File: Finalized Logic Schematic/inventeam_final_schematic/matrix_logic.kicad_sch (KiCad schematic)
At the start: 27 parts, among them J1 USB_C_Receptacle_PowerOnly_6P, J2 Conn_01x02, J3 Screw_Terminal_01x04, J4 JST Female, J5 JST Male, J6 JST Female, J7 JST Male, U1 LM66100DCK, U2 LM66100DCK

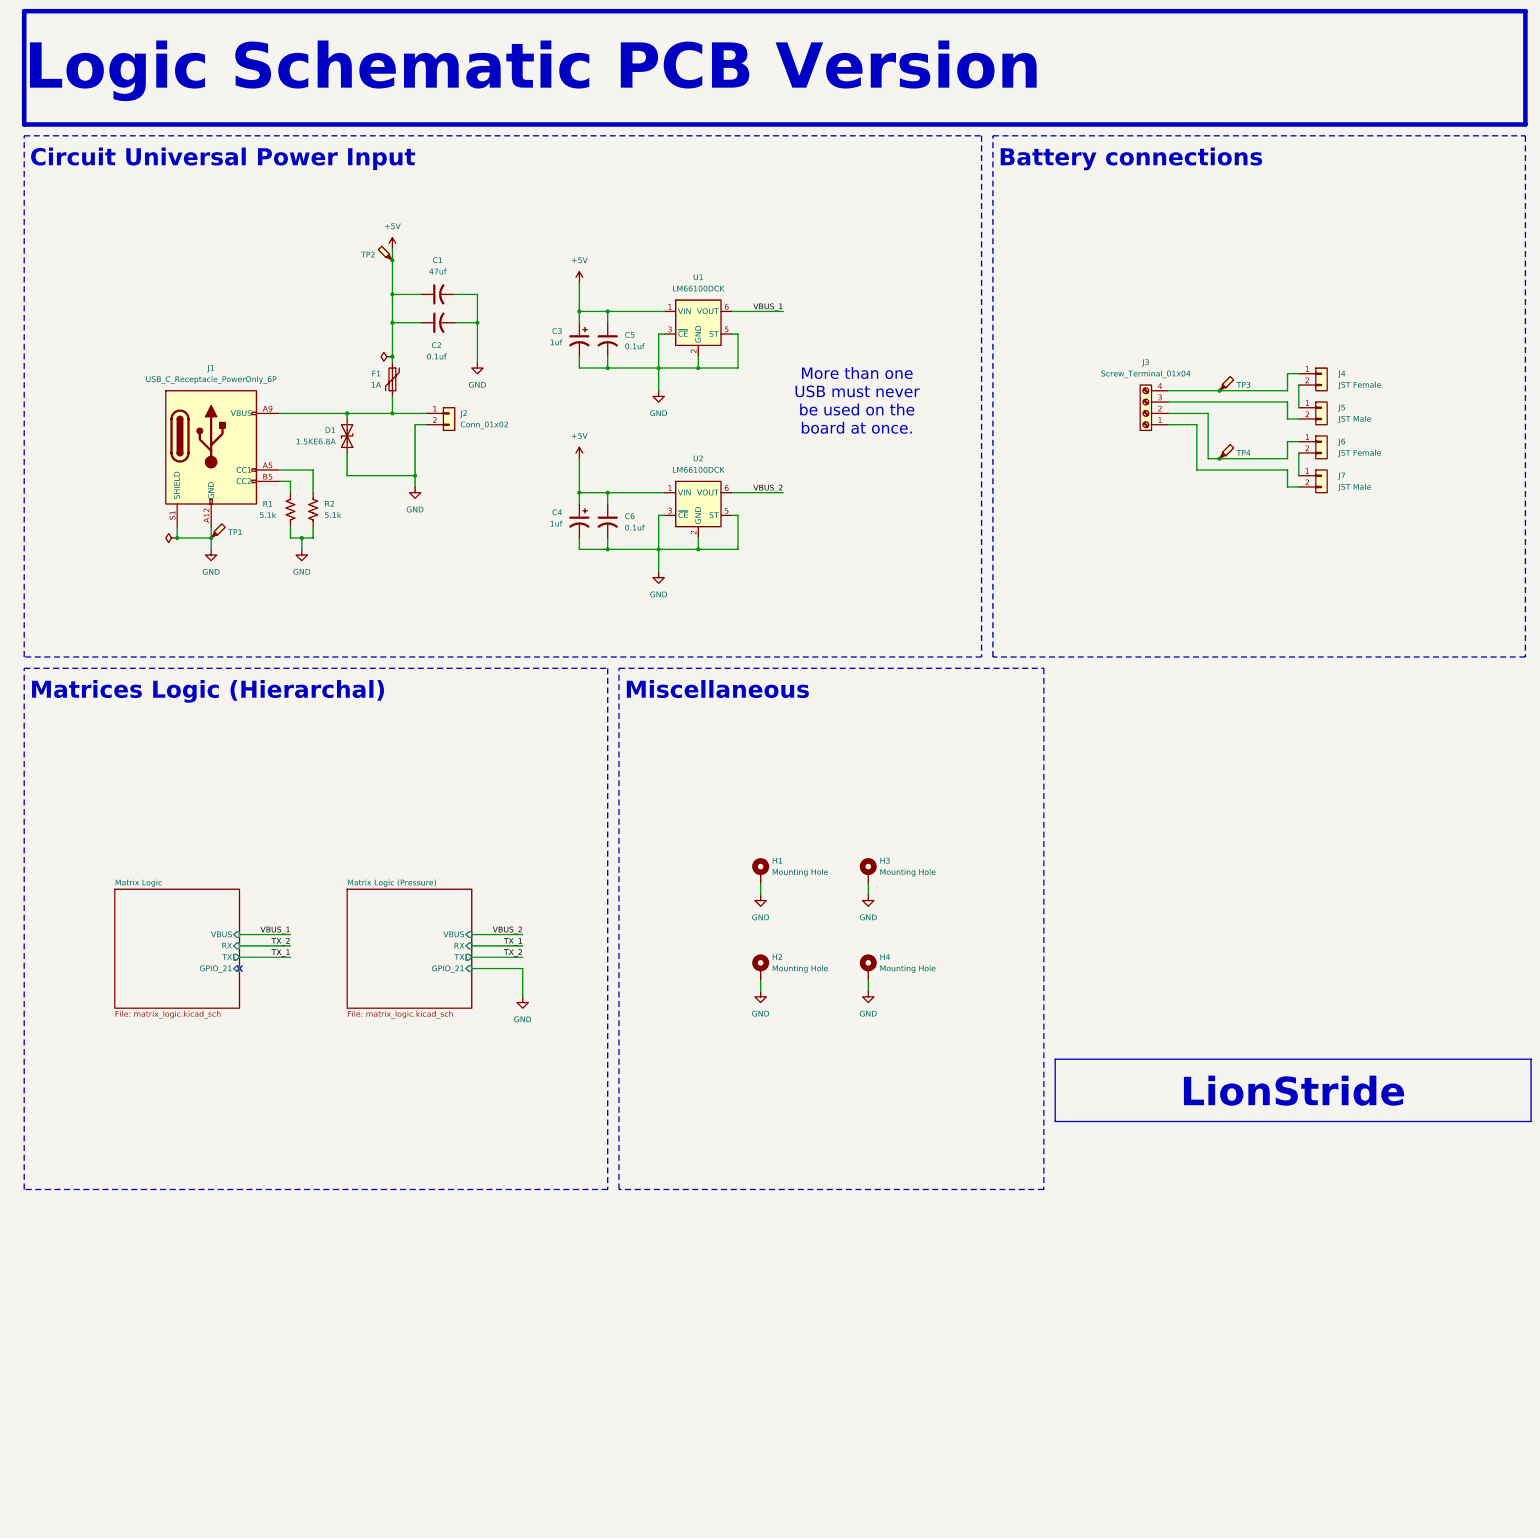
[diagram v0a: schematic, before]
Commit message: Logic schematic V2
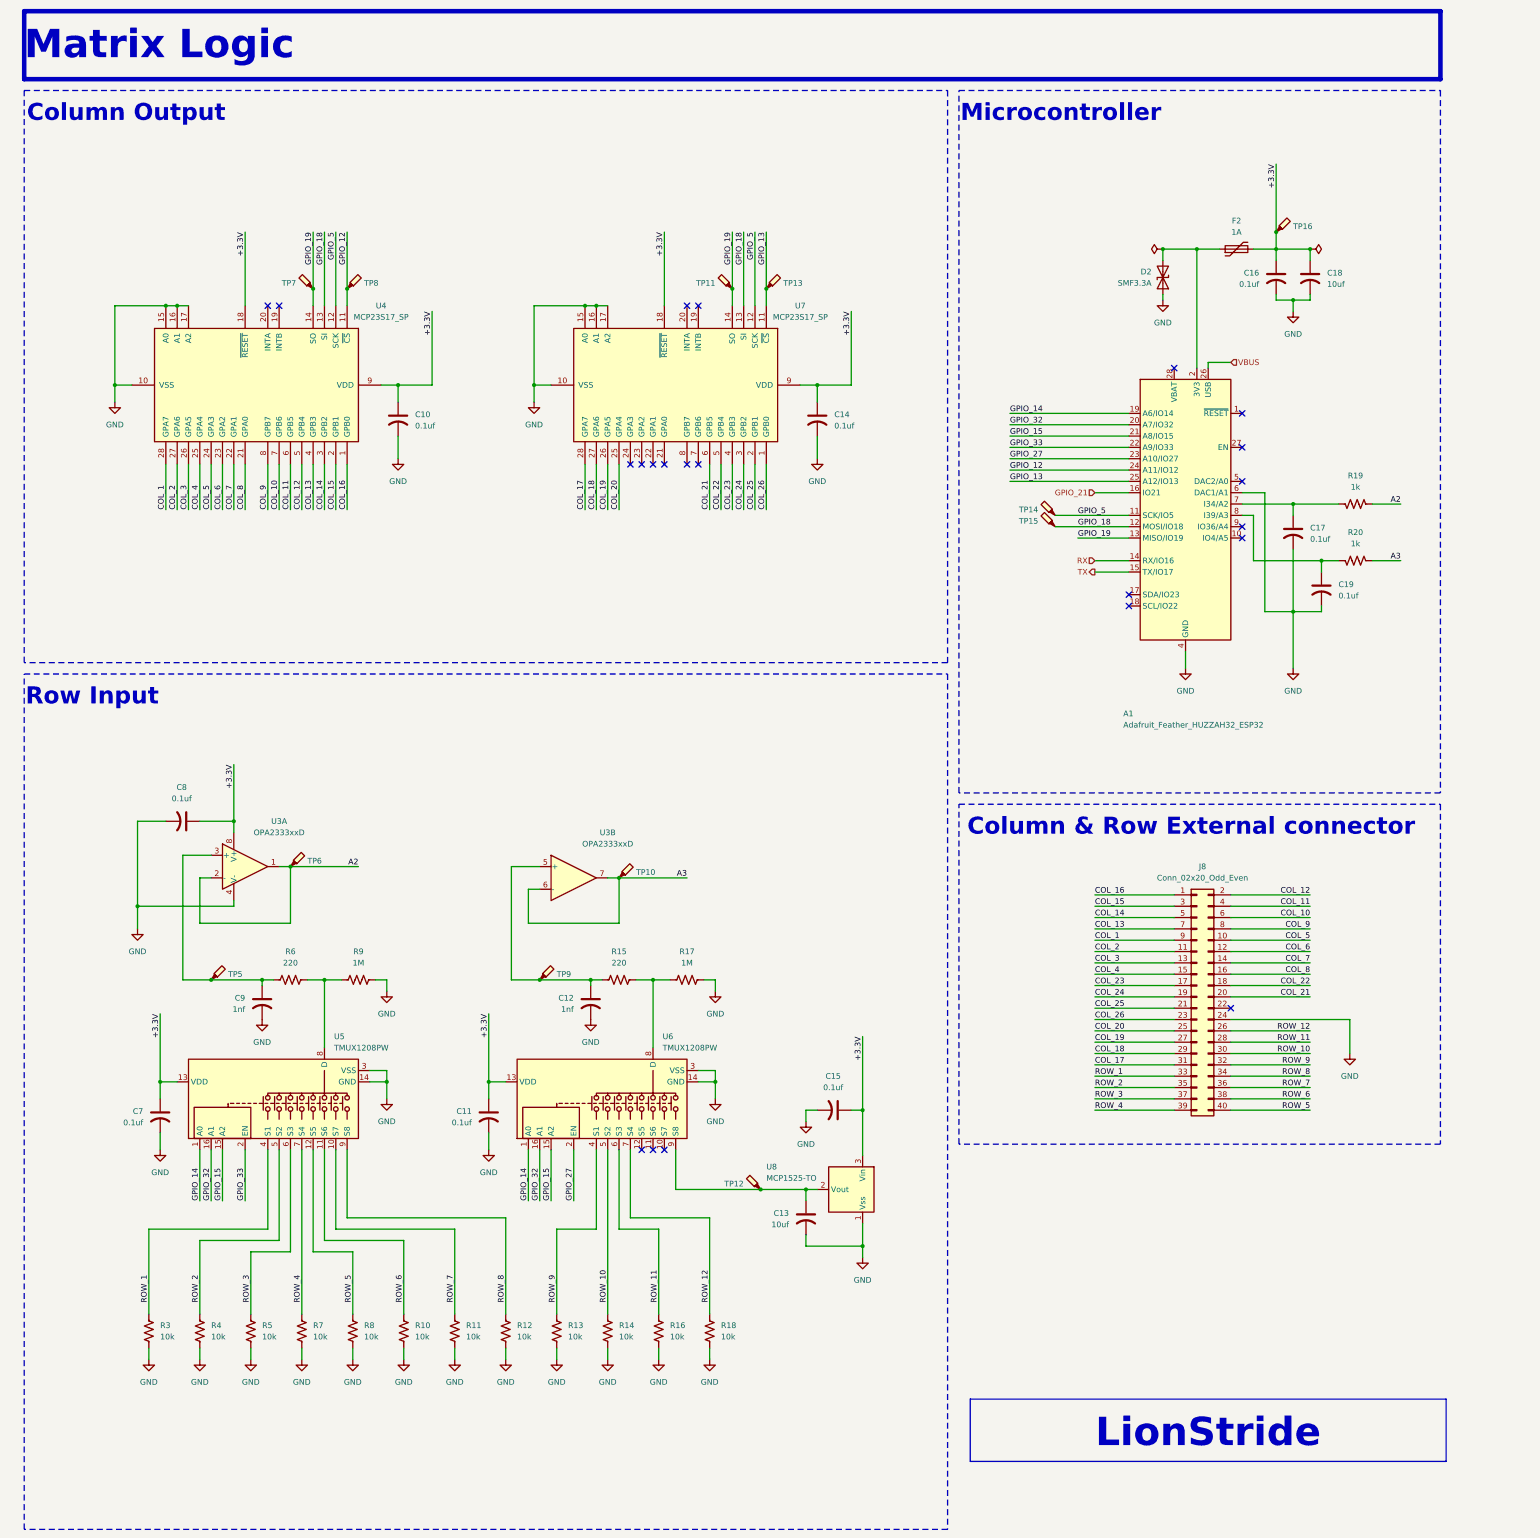
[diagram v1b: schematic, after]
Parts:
- removed C1: 47uf, Capacitor_THT:CP_Radial_D5.0mm_P2.50mm, symbol Device:C_US
- removed C2, C5, C6: 0.1uf, Capacitor_THT:C_Disc_D5.0mm_W2.5mm_P5.00mm, symbol Device:C_US
- removed C3, C4: 1uf, Capacitor_THT:CP_Axial_L10.0mm_D4.5mm_P15.00mm_Horizontal, symbol Device:C_Polarized_US
- removed D1: 1.5KE6.8A, Diode_THT:D_DO-201_P15.24mm_Horizontal, symbol Device:D_TVS
- removed F1: 1A, X16_GF100_PPTC:X16 GF100, symbol Device:Polyfuse
- removed H1, H2, H3, H4: Mounting Hole, MountingHole:MountingHole_2.5mm_Pad, symbol Mechanical:MountingHole_Pad
- removed J1: USB_C_Receptacle_PowerOnly_6P, Connector_USB:USB_C_Receptacle_GCT_USB4125-xx-x_6P_TopMnt_Horizontal, symbol Connector:USB_C_Receptacle_PowerOnly_6P
- removed J2: Conn_01x02, Connector_PinHeader_2.54mm:PinHeader_1x02_P2.54mm_Vertical, symbol Connector_Generic:Conn_01x02
- removed J3: Screw_Terminal_01x04, TerminalBlock:TerminalBlock_Xinya_XY308-2.54-4P_1x04_P2.54mm_Horizontal, symbol Connector:Screw_Terminal_01x04
- removed J4, J6: JST Female, Connector_PinHeader_2.54mm:PinHeader_1x02_P2.54mm_Vertical, symbol Connector_Generic:Conn_01x02
- removed J5, J7: JST Male, Connector_PinHeader_2.54mm:PinHeader_1x02_P2.54mm_Vertical, symbol Connector_Generic:Conn_01x02
- removed R1, R2: 5.1k, Resistor_THT:R_Axial_DIN0207_L6.3mm_D2.5mm_P7.62mm_Horizontal, symbol Device:R_US
- removed TP1, TP2, TP3, TP4: TestPoint_Probe, TestPoint:TestPoint_Pad_D1.0mm, symbol Connector:TestPoint_Probe
- removed U1, U2: LM66100DCK, Package_TO_SOT_SMD:SOT-363_SC-70-6, symbol Power_Management:LM66100DCK
- added A1: Adafruit_Feather_HUZZAH32_ESP32, Module:Adafruit_Feather, symbol MCU_Module:Adafruit_Feather_HUZZAH32_ESP32
- added C10, C11, C14, C15, C16, C17, C19, C7, C8: 0.1uf, Capacitor_THT:C_Disc_D5.0mm_W2.5mm_P5.00mm, symbol Device:C_US
- added C12, C9: 1nf, Capacitor_THT:CP_Axial_L10.0mm_D4.5mm_P15.00mm_Horizontal, symbol Device:C_US
- added C13, C18: 10uf, Capacitor_THT:C_Disc_D5.0mm_W2.5mm_P2.50mm, symbol Device:C_US
- added D2: SMF3.3A, Diode_SMD:D_SOD-123F, symbol Device:D_TVS
- added F2: 1A, X16_GF100_PPTC:X16 GF100, symbol Device:Polyfuse
- added J8: Conn_02x20_Odd_Even, Connector_PinHeader_2.54mm:PinHeader_2x20_P2.54mm_Vertical, symbol Connector_Generic:Conn_02x20_Odd_Even
- added R10, R11, R12, R13, R14, R16, R18, R3, R4, R5, R7, R8: 10k, Resistor_THT:R_Axial_DIN0207_L6.3mm_D2.5mm_P7.62mm_Horizontal, symbol Device:R_US
- added R15, R6: 220, Resistor_THT:R_Axial_DIN0207_L6.3mm_D2.5mm_P10.16mm_Horizontal, symbol Device:R_US
- added R17, R9: 1M, Resistor_THT:R_Axial_DIN0207_L6.3mm_D2.5mm_P7.62mm_Horizontal, symbol Device:R_US
- added R19, R20: 1k, Resistor_THT:R_Axial_DIN0207_L6.3mm_D2.5mm_P7.62mm_Horizontal, symbol Device:R_US
- added TP10, TP11, TP12, TP13, TP14, TP15, TP16, TP5, TP6, TP7, TP8, TP9: TestPoint_Probe, TestPoint:TestPoint_Pad_D1.0mm, symbol Connector:TestPoint_Probe
- added U3: OPA2333xxD, Package_SO:SOIC-8_3.9x4.9mm_P1.27mm, symbol Amplifier_Operational:OPA2333xxD
- added U4, U7: MCP23S17_SP, Package_DIP:DIP-28_W7.62mm, symbol Interface_Expansion:MCP23S17_SP
- added U5, U6: TMUX1208PW, Package_SO:TSSOP-16_4.4x5mm_P0.65mm, symbol Analog_Switch:TMUX1208PW
- added U8: MCP1525-TO, Package_TO_SOT_THT:TO-92_Inline, symbol Reference_Voltage:MCP1525-TO
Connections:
- net GND: now also A1.4 (GND), A1.6 (DAC1/A1), C10.2, C11.2, C12.2, C13.2, C14.2, C15.2, C16.2, C17.2, C18.2, C19.2, C7.2, C8.2, C9.2, D2.1 (A1), J8.24 (Pin_24), R10.2, R11.2, R12.2, R13.2, R14.2, R16.2, R17.2, R18.2, R3.2, R4.2, R5.2, R7.2, R8.2, R9.2, U3.4 (V-), U4.10 (VSS), U4.15 (A0), U4.16 (A1), U4.17 (A2), U5.14 (GND), U5.3 (VSS), U6.14 (GND), U6.3 (VSS), U7.10 (VSS), U7.15 (A0), U7.16 (A1), U7.17 (A2), U8.1 (Vss)
- new net: C12.1, R15.1, TP9.1, U3.5 (+)
- new net: C9.1, R6.1, TP5.1, U3.3 (+)
- new net: R6.2, R9.1, U5.8 (D)
- new net: A1.8 (I39/A3), C19.1, R20.2
- new net: R15.2, R17.1, U6.8 (D)
- new net: A1.7 (I34/A2), C17.1, R19.2
- new net: C13.1, TP12.1, U6.9 (S8), U8.2 (Vout)
- new net: A1.2 (3V3), D2.2 (A2), F2.1
- new net +3.3V: C10.1, C11.1, C14.1, C15.1, C16.1, C18.1, C7.1, C8.1, F2.2, TP16.1, U3.8 (V+), U4.18 (~{RESET}), U4.9 (VDD), U5.13 (VDD), U6.13 (VDD), U7.18 (~{RESET}), U7.9 (VDD), U8.3 (Vin)
- new net A2: R19.1, TP6.1, U3.1, U3.2 (-)
- new net A3: R20.1, TP10.1, U3.6 (-), U3.7
- new net COL_1: J8.9 (Pin_9), U4.28 (GPA7)
- new net COL_10: J8.6 (Pin_6), U4.7 (GPB6)
- new net COL_11: J8.4 (Pin_4), U4.6 (GPB5)
- new net COL_12: J8.2 (Pin_2), U4.5 (GPB4)
- new net COL_13: J8.7 (Pin_7), U4.4 (GPB3)
- new net COL_14: J8.5 (Pin_5), U4.3 (GPB2)
- new net COL_15: J8.3 (Pin_3), U4.2 (GPB1)
- new net COL_16: J8.1 (Pin_1), U4.1 (GPB0)
- new net COL_17: J8.31 (Pin_31), U7.28 (GPA7)
- new net COL_18: J8.29 (Pin_29), U7.27 (GPA6)
- new net COL_19: J8.27 (Pin_27), U7.26 (GPA5)
- new net COL_2: J8.11 (Pin_11), U4.27 (GPA6)
- new net COL_20: J8.25 (Pin_25), U7.25 (GPA4)
- new net COL_21: J8.20 (Pin_20), U7.6 (GPB5)
- new net COL_22: J8.18 (Pin_18), U7.5 (GPB4)
- new net COL_23: J8.17 (Pin_17), U7.4 (GPB3)
- new net COL_24: J8.19 (Pin_19), U7.3 (GPB2)
- new net COL_25: J8.21 (Pin_21), U7.2 (GPB1)
- new net COL_26: J8.23 (Pin_23), U7.1 (GPB0)
- new net COL_3: J8.13 (Pin_13), U4.26 (GPA5)
- new net COL_4: J8.15 (Pin_15), U4.25 (GPA4)
- new net COL_5: J8.10 (Pin_10), U4.24 (GPA3)
- new net COL_6: J8.12 (Pin_12), U4.23 (GPA2)
- new net COL_7: J8.14 (Pin_14), U4.22 (GPA1)
- new net COL_8: J8.16 (Pin_16), U4.21 (GPA0)
- new net COL_9: J8.8 (Pin_8), U4.8 (GPB7)
- new net GPIO_12: A1.24 (A11/IO12), TP8.1, U4.11 (~{CS})
- new net GPIO_13: A1.25 (A12/IO13), TP13.1, U7.11 (~{CS})
- new net GPIO_14: A1.19 (A6/IO14), U5.1 (A0), U6.1 (A0)
- new net GPIO_15: A1.21 (A8/IO15), U5.15 (A2), U6.15 (A2)
- new net GPIO_18: A1.12 (MOSI/IO18), TP15.1, U4.13 (SI), U7.13 (SI)
- new net GPIO_19: A1.13 (MISO/IO19), TP11.1, TP7.1, U4.14 (SO), U7.14 (SO)
- new net GPIO_21: A1.16 (IO21)
- new net GPIO_27: A1.23 (A10/IO27), U6.2 (EN)
- new net GPIO_32: A1.20 (A7/IO32), U5.16 (A1), U6.16 (A1)
- new net GPIO_33: A1.22 (A9/IO33), U5.2 (EN)
- new net GPIO_5: A1.11 (SCK/IO5), TP14.1, U4.12 (SCK), U7.12 (SCK)
- new net ROW_1: J8.33 (Pin_33), R3.1, U5.4 (S1)
- new net ROW_10: J8.30 (Pin_30), R14.1, U6.5 (S2)
- new net ROW_11: J8.28 (Pin_28), R16.1, U6.6 (S3)
- new net ROW_12: J8.26 (Pin_26), R18.1, U6.7 (S4)
- new net ROW_2: J8.35 (Pin_35), R4.1, U5.5 (S2)
- new net ROW_3: J8.37 (Pin_37), R5.1, U5.6 (S3)
- new net ROW_4: J8.39 (Pin_39), R7.1, U5.7 (S4)
- new net ROW_5: J8.40 (Pin_40), R8.1, U5.12 (S5)
- new net ROW_6: J8.38 (Pin_38), R10.1, U5.11 (S6)
- new net ROW_7: J8.36 (Pin_36), R11.1, U5.10 (S7)
- new net ROW_8: J8.34 (Pin_34), R12.1, U5.9 (S8)
- new net ROW_9: J8.32 (Pin_32), R13.1, U6.4 (S1)
- new net RX: A1.14 (RX/IO16)
- new net TX: A1.15 (TX/IO17)
- new net VBUS: A1.26 (USB)
- no-connect marks 1 -> 22
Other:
- removed sheet Matrix Logic
- removed sheet Matrix Logic (Pressure)
- note added: "Column & Row External connector"
- note added: "Column Output"
- note added: "Matrix Logic"
- note added: "Microcontroller"
- note added: "Row Input"
- note removed: "Battery connections"
- note removed: "Circuit Universal Power Input"
- note removed: "Logic Schematic PCB Version"
- note removed: "Matrices Logic (Hierarchal)"
- note removed: "Miscellaneous"
- note removed: "More than one USB must never be used on the board at once."
- title: Logic Schematic -> Matrix Logic

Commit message: Logic schematic V3
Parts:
- removed A1: Adafruit_Feather_HUZZAH32_ESP32, Module:Adafruit_Feather, symbol MCU_Module:Adafruit_Feather_HUZZAH32_ESP32
- removed C16, C17, C19: 0.1uf, Capacitor_THT:C_Disc_D5.0mm_W2.5mm_P5.00mm, symbol Device:C_US
- removed C18: 10uf, Capacitor_THT:C_Disc_D5.0mm_W2.5mm_P2.50mm, symbol Device:C_US
- removed D2: SMF3.3A, Diode_SMD:D_SOD-123F, symbol Device:D_TVS
- removed F2: 1A, X16_GF100_PPTC:X16 GF100, symbol Device:Polyfuse
- removed R19, R20: 1k, Resistor_THT:R_Axial_DIN0207_L6.3mm_D2.5mm_P7.62mm_Horizontal, symbol Device:R_US
- removed TP14, TP15, TP16: TestPoint_Probe, TestPoint:TestPoint_Pad_D1.0mm, symbol Connector:TestPoint_Probe
- renumbered C11 to C10, C12 to C11, C13 to C12, C15 to C13, C10 to C14, C14 to C15, J8 to J2, R8 to R10, R9 to R11, R10 to R12, R11 to R13, R12 to R14, R13 to R15, R14 to R16, R15 to R17, R16 to R18, R17 to R19, R18 to R20, R3 to R5, R4 to R6, R5 to R7, R6 to R8, R7 to R9, TP7 to TP10, TP8 to TP11, TP11 to TP12, TP9 to TP7, TP10 to TP8, TP12 to TP9, U3 to U1, U5 to U2, U6 to U3, U8 to U4, U4 to U5, U7 to U6
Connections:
- net A2 renamed ROW_OUT_1
- net A3 renamed ROW_OUT_2
- net GPIO_12 renamed CS_1
- net GPIO_13 renamed CS_2
- net GPIO_14 renamed MUX_A0
- net GPIO_15 renamed MUX_A2
- net GPIO_18 renamed MOSI
- net GPIO_19 renamed MISO
- net GPIO_27 renamed MUX_EN_2
- net GPIO_32 renamed MUX_A1
- net GPIO_33 renamed MUX_EN_1
- net GPIO_5 renamed SCK
- no-connect marks 22 -> 14
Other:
- note added: "External connector"
- note removed: "Column & Row External connector"
- note removed: "Microcontroller"
- moved on the sheet: C10, C11, C12, C13, C14, C15, C7, C8, C9, J2, R10, R11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
